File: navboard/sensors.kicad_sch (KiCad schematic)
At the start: 24 parts, among them SW1 SW_Push, U1 LIS3MDL, U2 SHT35-DIS, U3 BMI088, U4 ICM-42688-P, U5 BMM150, U6 LSM9DS1

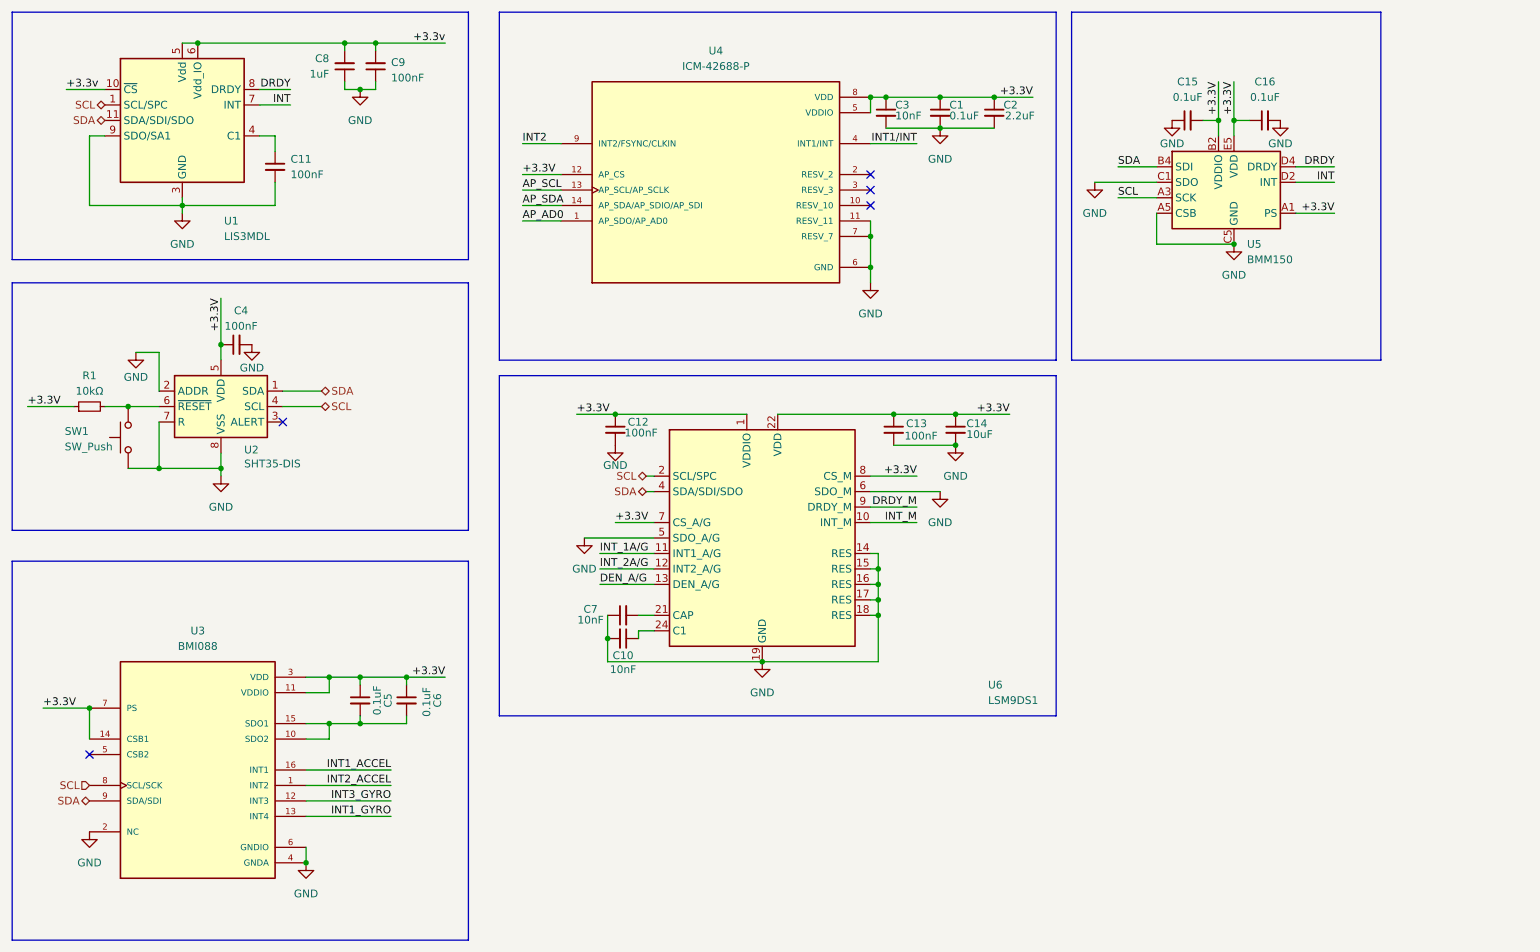
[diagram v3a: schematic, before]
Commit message: Feat[navboard]: Breakout of Different Sensors
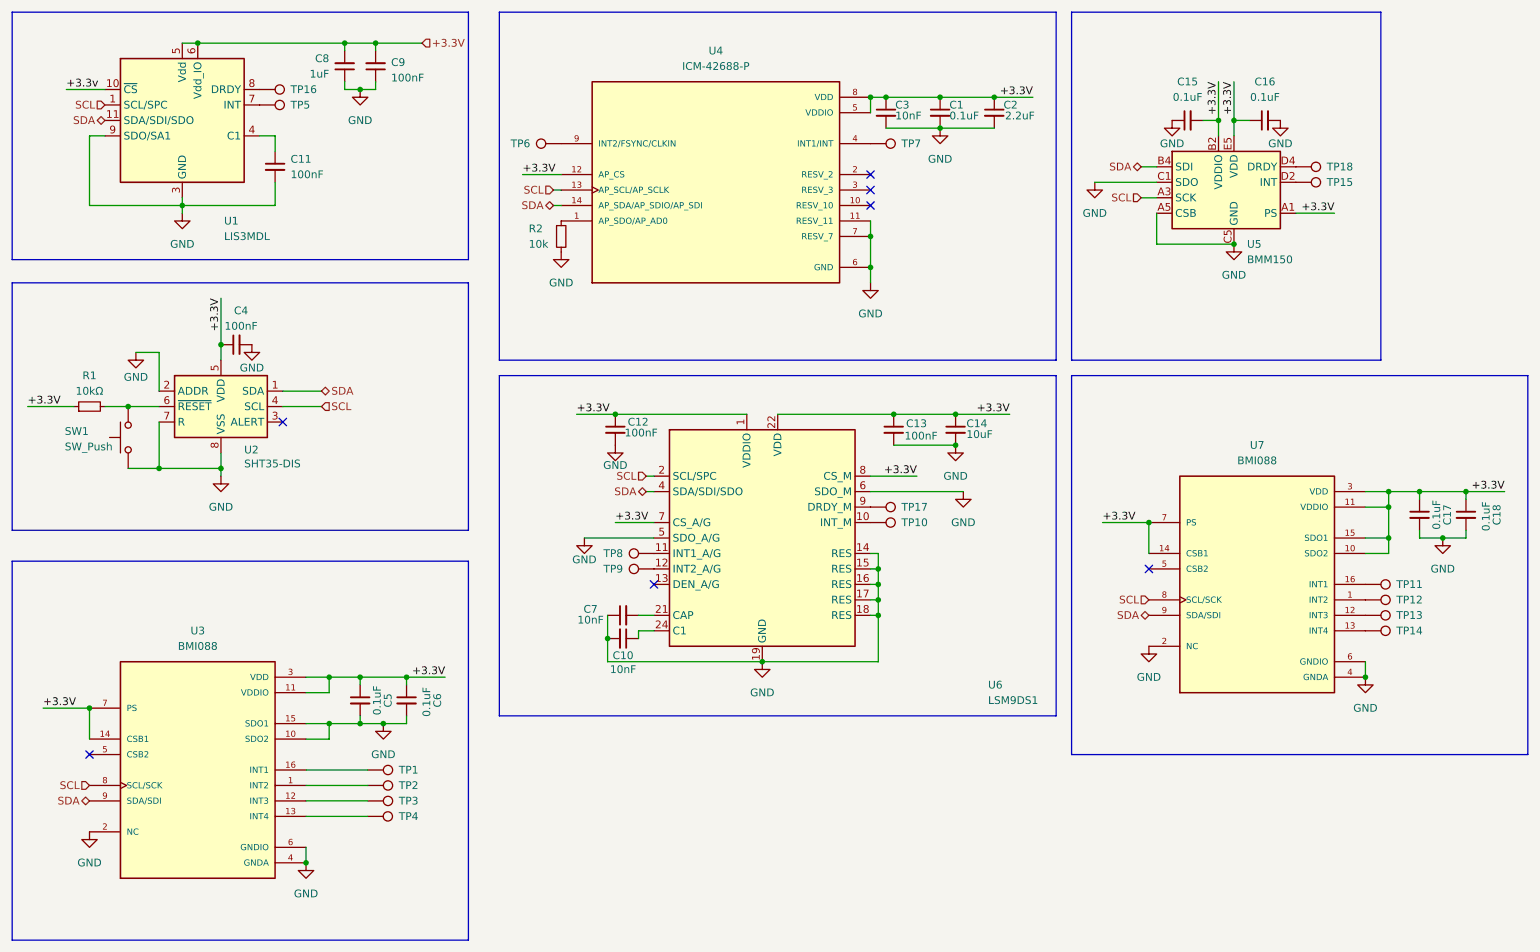
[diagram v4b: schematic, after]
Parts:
- added C17, C18: 0.1uF, Capacitor_SMD:C_0603_1608Metric, symbol Device:C_Small
- added R2: 10k, Resistor_SMD:R_0603_1608Metric, symbol Device:R_Small
- added TP1, TP10, TP11, TP12, TP13, TP14, TP15, TP16, TP17, TP18, TP2, TP3, TP4, TP5, TP6, TP7, TP8, TP9: TestPoint, TestPoint:TestPoint_Pad_D1.0mm, symbol Connector:TestPoint
- added U7: BMI088, PQFN50P450X300X100-16N, symbol BMI088:BMI088
- C1, C10, C12, C13, C14, C15, C16, C2, C3, C4, C5, C6, C7: footprint (none) -> Capacitor_SMD:C_0603_1608Metric
- C11, C8, C9: footprint Capacitor_SMD:C_0402_1005Metric -> Capacitor_SMD:C_0603_1608Metric
- R1: footprint (none) -> Resistor_SMD:R_0603_1608Metric
- SW1: footprint (none) -> Button_Switch_SMD:SW_Push_SPST_NO_Alps_SKRK
- U4: footprint ICM-42688-P:PQFN50P300X250X97-14N -> ICM-42688-P:LGA14_2P5X3X0P91_IVS
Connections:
- net AP_SCL is gone; now on net SCL: U4.13 (AP_SCL/AP_SCLK)
- net AP_SDA is gone; now on net SDA: U4.14 (AP_SDA/AP_SDIO/AP_SDI)
- net +3.3V: now also C8.2, C9.2, U1.5 (Vdd), U1.6 (Vdd_IO), C17.1, C18.1, U7.10 (SDO2), U7.11 (VDDIO), U7.14 (CSB1), U7.15 (SDO1), U7.3 (VDD), U7.7 (PS)
- net +3.3v: no longer C8.2, C9.2, U1.5 (Vdd), U1.6 (Vdd_IO)
- net GND: now also C5.2, C6.2, U3.10 (SDO2), U3.15 (SDO1), C17.2, C18.2, R2.2, U7.2 (NC), U7.4 (GNDA), U7.6 (GNDIO)
- net SCL: now also U7.8 (SCL/SCK)
- net SDA: now also U7.9 (SDA/SDI)
- net AP_AD0: no longer names the net of U4.1 (AP_SDO/AP_AD0)
- net AP_AD0: now also R2.1
- net DEN_A/G: no longer names the net of U6.13 (DEN_A/G)
- net DRDY: no longer names the net of U5.D4 (DRDY)
- net DRDY: now also TP18.1; no longer U1.8 (DRDY)
- net DRDY_M: no longer names the net of U6.9 (DRDY_M)
- net DRDY_M: now also TP17.1
- net INT: no longer names the net of U1.7 (INT)
- net INT: now also TP5.1; no longer U5.D2 (INT)
- net INT1_ACCEL: no longer names the net of U3.16 (INT1)
- net INT1_ACCEL: now also TP1.1
- net INT1_GYRO: no longer names the net of U3.13 (INT4)
- net INT1_GYRO: now also TP4.1
- net INT1/INT: no longer names the net of U4.4 (INT1/INT)
- net INT1/INT: now also TP7.1
- net INT2: no longer names the net of U4.9 (INT2/FSYNC/CLKIN)
- net INT2: now also TP6.1
- net INT2_ACCEL: no longer names the net of U3.1 (INT2)
- net INT2_ACCEL: now also TP2.1
- net INT3_GYRO: no longer names the net of U3.12 (INT3)
- net INT3_GYRO: now also TP3.1
- net INT_1A/G: no longer names the net of U6.11 (INT1_A/G)
- net INT_1A/G: now also TP8.1
- net INT_2A/G: no longer names the net of U6.12 (INT2_A/G)
- net INT_2A/G: now also TP9.1
- net INT_M: no longer names the net of U6.10 (INT_M)
- net INT_M: now also TP10.1
- new net: TP15.1, U5.D2 (INT)
- new net: TP16.1, U1.8 (DRDY)
- new net: TP13.1, U7.12 (INT3)
- new net: TP12.1, U7.1 (INT2)
- new net: TP14.1, U7.13 (INT4)
- new net: TP11.1, U7.16 (INT1)
- no-connect marks 5 -> 7
